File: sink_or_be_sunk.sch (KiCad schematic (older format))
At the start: 49 parts, among them J1 Battery_Conn, J10 SWD_Conn, J11 USB_B_Micro, J2 Display_Conn, J3 Keypad_Conn, J4 Mux_Conn, M1 Motor_DC, Q1 IRLML5203, Q2 MMBT5550L, Q3 MMBT5550L, SW4 Reset_SW, U1 ESP32-WROOM-32, U2 MCP608, U3 SN74HC151N, U6 LDL1117-SMD, U7 CY7C65213A-28PVXI, U8 MCP73831-2-OT

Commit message: cleaned up project
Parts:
- C1: renamed from C17; footprint Capacitor_SMD:C_0805_2012Metric_Pad1.15x1.40mm_HandSolder -> Capacitor_SMD:C_0805_2012Metric_Pad1.18x1.45mm_HandSolder
- C2: renamed from C18; footprint Capacitor_SMD:C_0805_2012Metric_Pad1.15x1.40mm_HandSolder -> Capacitor_SMD:C_0805_2012Metric_Pad1.18x1.45mm_HandSolder
- H1, H2, H3, H4: footprint MountingHole:MountingHole_6.4mm_M6 -> MountingHole:MountingHole_3.2mm_M3
- J6: renamed from J11; footprint digikey-footprints:USB_Micro_B_Female_Vert_1051330001 -> PCB_ESP32:USB_Micro_B_Female_Vert_1051330001
- R1, R2, R3: footprint Resistor_SMD:R_0805_2012Metric_Pad1.15x1.40mm_HandSolder -> Resistor_SMD:R_0805_2012Metric_Pad1.20x1.40mm_HandSolder
- R11: renamed from R22; footprint Resistor_SMD:R_0805_2012Metric_Pad1.15x1.40mm_HandSolder -> Resistor_SMD:R_0805_2012Metric_Pad1.20x1.40mm_HandSolder
- R7: renamed from R16; footprint Resistor_SMD:R_0805_2012Metric_Pad1.15x1.40mm_HandSolder -> Resistor_SMD:R_0805_2012Metric_Pad1.20x1.40mm_HandSolder
- R8: renamed from R17; footprint Resistor_SMD:R_0805_2012Metric_Pad1.15x1.40mm_HandSolder -> Resistor_SMD:R_0805_2012Metric_Pad1.20x1.40mm_HandSolder
- renumbered C22 to C10, C25 to C11, C23 to C3, C24 to C4, C19 to C5, C16 to C6, C1 to C7, C20 to C8, C21 to C9, D6 to D1, D1 to D2, D4 to D3, D5 to D4, J3 to J1, J4 to J2, J2 to J3, J10 to J4, J1 to J5, R19 to R10, R20 to R5, R21 to R6, R18 to R9, SW4 to SW1, U3 to U1, U6 to U2, U8 to U3, U2 to U4, U1 to U5, U7 to U6
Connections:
- net labels removed: VDD

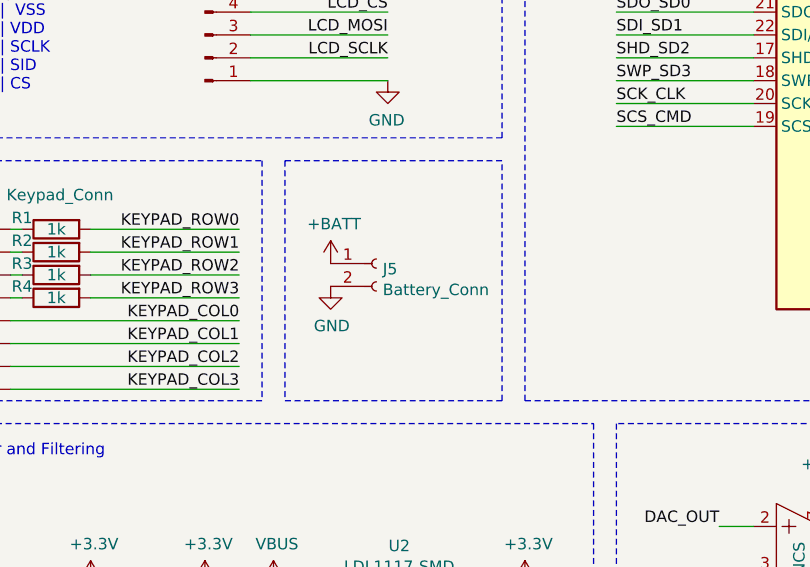
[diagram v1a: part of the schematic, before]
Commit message: added electrical isoltion switch
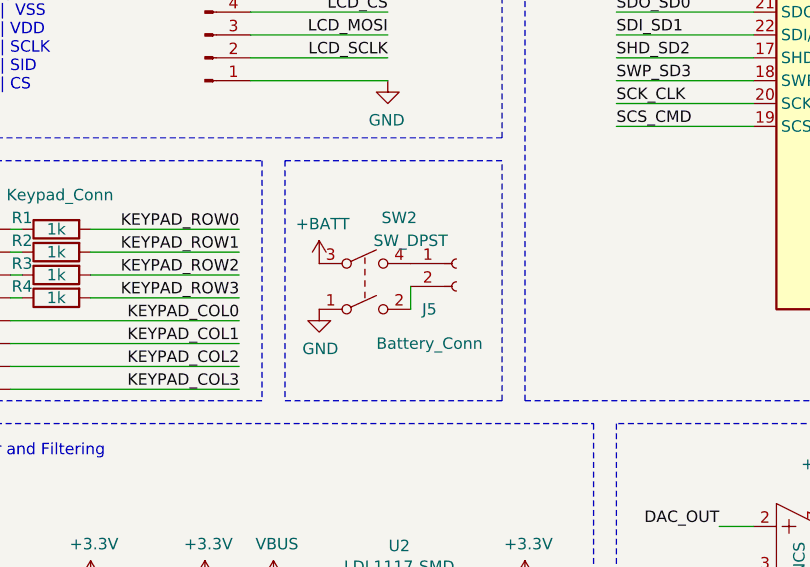
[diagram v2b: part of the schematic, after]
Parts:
- added SW2: SW_DPST, Connector_PinHeader_2.54mm:PinHeader_1x04_P2.54mm_Horizontal, symbol Switch:SW_DPST
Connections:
- wire segments 186 -> 187
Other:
- moved on the sheet: J5
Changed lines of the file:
@@
 L power:+BATT #PWR09
 U 1 1 622D2577
-P 2350 3350
-F 0 "#PWR09" H 2350 3200 50  0001 C CNN
-F 1 "+BATT" H 2365 3523 50  0000 C CNN
-F 2 "" H 2350 3350 50  0001 C CNN
-F 3 "" H 2350 3350 50  0001 C CNN
-	1    2350 3350
+P 2300 3350
+F 0 "#PWR09" H 2300 3200 50  0001 C CNN
+F 1 "+BATT" H 2315 3523 50  0000 C CNN
+F 2 "" H 2300 3350 50  0001 C CNN
+F 3 "" H 2300 3350 50  0001 C CNN
+	1    2300 3350
 	1    0    0    -1
 $EndComp
@@
 L power:GND #PWR010
 U 1 1 6239E5F9
-P 2350 3450
-F 0 "#PWR010" H 2350 3200 50  0001 C CNN
-F 1 "GND" H 2355 3277 50  0000 C CNN
-F 2 "" H 2350 3450 50  0001 C CNN
-F 3 "" H 2350 3450 50  0001 C CNN
-	1    2350 3450
+P 2300 3550
+F 0 "#PWR010" H 2300 3300 50  0001 C CNN
+F 1 "GND" H 2305 3377 50  0000 C CNN
+F 2 "" H 2300 3550 50  0001 C CNN
+F 3 "" H 2300 3550 50  0001 C CNN
+	1    2300 3550
 	1    0    0    -1
 $EndComp
@@
 L Connector:Conn_01x02_Female J5
 U 1 1 623CFEBF
-P 2550 3350
-F 0 "J5" H 2578 3326 50  0000 L CNN
-F 1 "Battery_Conn" H 2578 3235 50  0000 L CNN
-F 2 "Connector_JST:JST_PH_S2B-PH-K_1x02_P2.00mm_Horizontal" H 2550 3350 50  0001 C CNN
-F 3 "~" H 2550 3350 50  0001 C CNN
-	1    2550 3350
+P 2900 3350
+F 0 "J5" H 2750 3150 50  0000 L CNN
+F 1 "Battery_Conn" H 2550 3000 50  0000 L CNN
+F 2 "Connector_JST:JST_PH_S2B-PH-K_1x02_P2.00mm_Horizontal" H 2900 3350 50  0001 C CNN
+F 3 "~" H 2900 3350 50  0001 C CNN
+	1    2900 3350
 	1    0    0    -1
 $EndComp
@@
 	7400 5950 7650 5950
 $Comp
-L power:+3.3V #PWR?
+L power:+3.3V #PWR015
 U 1 1 61610F9E
 P 4500 4400
-F 0 "#PWR?" H 4500 4250 50  0001 C CNN
+F 0 "#PWR015" H 4500 4250 50  0001 C CNN
 F 1 "+3.3V" H 4515 4573 50  0000 C CNN
 F 2 "" H 4500 4400 50  0001 C CNN
@@
 	1    0    0    -1
 $EndComp
+$Comp
+L Switch:SW_DPST SW2
+U 1 1 615EE1A6
+P 2500 3450
+F 0 "SW2" H 2650 3750 50  0000 C CNN
+F 1 "SW_DPST" H 2700 3650 50  0000 C CNN
+F 2 "Connector_PinHeader_2.54mm:PinHeader_1x04_P2.54mm_Horizontal" H 2500 3450 50  0001 C CNN
+F 3 "~" H 2500 3450 50  0001 C CNN
+	1    2500 3450
+	1    0    0    -1
+$EndComp
+Wire Wire Line
+	2700 3450 2700 3550
 $EndSCHEMATC

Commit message: redo of layout and minor circuit updates
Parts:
- removed D2: D_Zener, Diode_SMD:D_0805_2012Metric_Pad1.15x1.40mm_HandSolder, symbol Device:D_Zener
- added C12: 10uF, Capacitor_THT:CP_Radial_D8.0mm_P3.50mm, symbol Device:C
- added D2: D, Diode_THT:D_DO-15_P10.16mm_Horizontal, symbol Device:D
- C7: footprint Capacitor_SMD:C_0805_2012Metric_Pad1.15x1.40mm_HandSolder -> Capacitor_THT:CP_Radial_D8.0mm_P3.50mm
- J4: value SWD_Conn -> JTAG_Conn; footprint Connector_PinHeader_2.54mm:PinHeader_1x06_P2.54mm_Vertical -> Connector_PinHeader_2.54mm:PinHeader_1x04_P2.54mm_Vertical; symbol Connector:Conn_01x06_Male -> Connector:Conn_01x04_Male
- U1: footprint PCB_ESP32:SN74HC151N-PDIP -> Package_DIP:DIP-16_W10.16mm
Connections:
- net labels added: MTCK, MTDI, MTDO, MTMS
- net labels removed: SCK_CLK, SCS_CMD, SDI_SD1, SDO_SD0, SHD_SD2, SWP_SD3
- wire segments 187 -> 182
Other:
- note removed: "Using 7/16” standoff \n(11.13mm tall, 6.35mm diam)"
- moved on the sheet: H1, H2, H3, H4
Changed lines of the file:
@@
-$EndComp
-$Comp
-L Device:D_Zener D?
-U 1 1 61603AE8
-P 7050 4100
-AR Path="/6154AAA6/61603AE8" Ref="D?"  Part="1"
-AR Path="/61603AE8" Ref="D2"  Part="1"
-F 0 "D2" V 7004 4179 50  0000 L CNN
-F 1 "D_Zener" V 7095 4179 50  0000 L CNN
-F 2 "Diode_SMD:D_0805_2012Metric_Pad1.15x1.40mm_HandSolder" H 7050 4100 50  0001 C CNN
-F 3 "~" H 7050 4100 50  0001 C CNN
-	1    7050 4100
-	0    1    1    0
 $EndComp
 $Comp
@@
 Wire Wire Line
 	5650 4900 5650 5050
-Wire Wire Line
-	5800 4750 6100 4750
 $Comp
 L Device:Speaker LS?
@@
 Text Label 3600 1050 0    50   ~ 0
 RESET
-Text Label 3600 2750 0    50   ~ 0
-SCS_CMD
-Text Label 3600 2650 0    50   ~ 0
-SCK_CLK
-Text Label 3600 2550 0    50   ~ 0
-SWP_SD3
-Text Label 3600 2450 0    50   ~ 0
-SHD_SD2
-Text Label 3600 2350 0    50   ~ 0
-SDI_SD1
-Text Label 3600 2250 0    50   ~ 0
-SDO_SD0
-Wire Wire Line
-	3600 2750 4200 2750
-Wire Wire Line
-	3600 2650 4200 2650
-Wire Wire Line
-	3600 2550 4200 2550
-Wire Wire Line
-	3600 2450 4200 2450
-Wire Wire Line
-	3600 2350 4200 2350
-Wire Wire Line
-	3600 2250 4200 2250
 Wire Wire Line
 	3600 1350 4200 1350
@@
 Wire Wire Line
 	5400 1250 6150 1250
-Text Label 6150 1650 2    50   ~ 0
+Text Label 3450 2350 0    50   ~ 0
 LED_OUT
 Wire Wire Line
-	5400 1650 6150 1650
+	4200 2350 3450 2350
 Text Label 6150 3150 2    50   ~ 0
 KEYPAD_COL3
@@
 Wire Wire Line
 	5400 2750 6150 2750
-Text Label 6150 1950 2    50   ~ 0
+Text Label 3450 2750 0    50   ~ 0
 LCD_CS
 Wire Wire Line
-	5400 1950 6150 1950
-Text Label 6150 1850 2    50   ~ 0
+	4200 2750 3450 2750
+Text Label 3450 2650 0    50   ~ 0
 LCD_SCLK
 Wire Wire Line
-	5400 1850 6150 1850
-Text Label 6150 1750 2    50   ~ 0
+	4200 2650 3450 2650
+Text Label 3450 2250 0    50   ~ 0
 LCD_MOSI
 Wire Wire Line
-	5400 1750 6150 1750
+	4200 2250 3450 2250
 Text Label 6150 2650 2    50   ~ 0
 MUX_ROW_SEL2
@@
 F 0 "C7" H 7765 6146 50  0000 L CNN
 F 1 "100uF" H 7765 6055 50  0000 L CNN
-F 2 "Capacitor_SMD:C_0805_2012Metric_Pad1.15x1.40mm_HandSolder" H 7688 5950 50  0001 C CNN
+F 2 "Capacitor_THT:CP_Radial_D8.0mm_P3.50mm" H 7688 5950 50  0001 C CNN
 F 3 "~" H 7650 6100 50  0001 C CNN
 	1    7650 6100
@@
 	7650 6250 7400 6250
 Connection ~ 7400 6250
-Text Label 2900 1400 2    50   ~ 0
-SCS_CMD
-Wire Wire Line
-	2900 1400 2300 1400
-Wire Wire Line
-	2900 900  2300 900
 Wire Wire Line
 	2900 1000 2300 1000
@@
 Wire Wire Line
 	2900 1300 2300 1300
-Text Label 2900 900  2    50   ~ 0
-SDO_SD0
 Text Label 2900 1000 2    50   ~ 0
-SDI_SD1
+MTDO
 Text Label 2900 1100 2    50   ~ 0
-SHD_SD2
+MTCK
 Text Label 2900 1200 2    50   ~ 0
-SWP_SD3
+MTDI
 Text Label 2900 1300 2    50   ~ 0
-SCK_CLK
-$Comp
-L Connector:Conn_01x06_Male J4
+MTMS
+$Comp
+L Connector:Conn_01x04_Male J4
 U 1 1 615AFA5D
 P 2100 1200
 F 0 "J4" H 2150 650 50  0000 R CNN
-F 1 "SWD_Conn" H 2300 750 50  0000 R CNN
-F 2 "Connector_PinHeader_2.54mm:PinHeader_1x06_P2.54mm_Vertical" H 2100 1200 50  0001 C CNN
+F 1 "JTAG_Conn" H 2300 750 50  0000 R CNN
+F 2 "Connector_PinHeader_2.54mm:PinHeader_1x04_P2.54mm_Vertical" H 2100 1200 50  0001 C CNN
 F 3 "~" H 2100 1200 50  0001 C CNN
 	1    2100 1200
@@
 F 0 "U1" H 2000 5885 50  0000 C CNN
 F 1 "SN74HC151N" H 2000 5976 50  0000 C CNN
-F 2 "PCB_ESP32:SN74HC151N-PDIP" H 2050 6450 50  0001 C CNN
+F 2 "Package_DIP:DIP-16_W10.16mm" H 2050 6450 50  0001 C CNN
 F 3 "" H 2050 6450 50  0001 C CNN
 	1    2000 6450
@@
 Wire Notes Line
 	6700 5650 3600 5650
-Text Notes 8400 5800 0    50   ~ 0
-Using 7/16” standoff \n(11.13mm tall, 6.35mm diam)
 $Comp
 L Mechanical:MountingHole H1
 U 1 1 6160EB38
-P 8500 6000
-F 0 "H1" H 8600 6046 50  0000 L CNN
-F 1 "MountingHole" H 8600 5955 50  0000 L CNN
-F 2 "MountingHole:MountingHole_3.2mm_M3" H 8500 6000 50  0001 C CNN
-F 3 "~" H 8500 6000 50  0001 C CNN
-	1    8500 6000
+P 8500 5900
+F 0 "H1" H 8600 5946 50  0000 L CNN
+F 1 "MountingHole" H 8600 5855 50  0000 L CNN
+F 2 "MountingHole:MountingHole_3.2mm_M3" H 8500 5900 50  0001 C CNN
+F 3 "~" H 8500 5900 50  0001 C CNN
+	1    8500 5900
 	1    0    0    -1
 $EndComp
@@
 L Mechanical:MountingHole H2
 U 1 1 615F8D16
-P 8500 6250
-F 0 "H2" H 8600 6296 50  0000 L CNN
-F 1 "MountingHole" H 8600 6205 50  0000 L CNN
-F 2 "MountingHole:MountingHole_3.2mm_M3" H 8500 6250 50  0001 C CNN
-F 3 "~" H 8500 6250 50  0001 C CNN
-	1    8500 6250
+P 8500 6150
+F 0 "H2" H 8600 6196 50  0000 L CNN
+F 1 "MountingHole" H 8600 6105 50  0000 L CNN
+F 2 "MountingHole:MountingHole_3.2mm_M3" H 8500 6150 50  0001 C CNN
+F 3 "~" H 8500 6150 50  0001 C CNN
+	1    8500 6150
 	1    0    0    -1
 $EndComp
@@
 L Mechanical:MountingHole H3
 U 1 1 615F8FBE
-P 9250 6000
-F 0 "H3" H 9350 6046 50  0000 L CNN
-F 1 "MountingHole" H 9350 5955 50  0000 L CNN
-F 2 "MountingHole:MountingHole_3.2mm_M3" H 9250 6000 50  0001 C CNN
-F 3 "~" H 9250 6000 50  0001 C CNN
-	1    9250 6000
+P 9250 5900
+F 0 "H3" H 9350 5946 50  0000 L CNN
+F 1 "MountingHole" H 9350 5855 50  0000 L CNN
+F 2 "MountingHole:MountingHole_3.2mm_M3" H 9250 5900 50  0001 C CNN
+F 3 "~" H 9250 5900 50  0001 C CNN
+	1    9250 5900
 	1    0    0    -1
 $EndComp
@@
 L Mechanical:MountingHole H4
 U 1 1 615F94F8
-P 9250 6250
-F 0 "H4" H 9350 6296 50  0000 L CNN
-F 1 "MountingHole" H 9350 6205 50  0000 L CNN
-F 2 "MountingHole:MountingHole_3.2mm_M3" H 9250 6250 50  0001 C CNN
-F 3 "~" H 9250 6250 50  0001 C CNN
-	1    9250 6250
+P 9250 6150
+F 0 "H4" H 9350 6196 50  0000 L CNN
+F 1 "MountingHole" H 9350 6105 50  0000 L CNN
+F 2 "MountingHole:MountingHole_3.2mm_M3" H 9250 6150 50  0001 C CNN
+F 3 "~" H 9250 6150 50  0001 C CNN
+	1    9250 6150
 	1    0    0    -1
 $EndComp
@@
 Wire Wire Line
 	2700 3450 2700 3550
+Wire Wire Line
+	6150 1650 5400 1650
+Text Label 6150 1650 2    50   ~ 0
+MTDI
+Wire Wire Line
+	6150 1750 5400 1750
+Text Label 6150 1750 2    50   ~ 0
+MTCK
+Wire Wire Line
+	6150 1850 5400 1850
+Text Label 6150 1850 2    50   ~ 0
+MTMS
+Wire Wire Line
+	6150 1950 5400 1950
+Text Label 6150 1950 2    50   ~ 0
+MTDO
+$Comp
+L Device:D D2
+U 1 1 616C0DF1
+P 7050 4100
+F 0 "D2" V 7004 4180 50  0000 L CNN
+F 1 "D" V 7095 4180 50  0000 L CNN
+F 2 "Diode_THT:D_DO-15_P10.16mm_Horizontal" H 7050 4100 50  0001 C CNN
+F 3 "https://www.diodes.com/assets/Datasheets/ds28002.pdf" H 7050 4100 50  0001 C CNN
+	1    7050 4100
+	0    1    1    0
+$EndComp
+$Comp
+L Device:C C12
+U 1 1 616DDA5F
+P 5950 4750
+F 0 "C12" V 5698 4750 50  0000 C CNN
+F 1 "10uF" V 5789 4750 50  0000 C CNN
+F 2 "Capacitor_THT:CP_Radial_D8.0mm_P3.50mm" H 5988 4600 50  0001 C CNN
+F 3 "~" H 5950 4750 50  0001 C CNN
+	1    5950 4750
+	0    1    1    0
+$EndComp
 $EndSCHEMATC

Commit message: 10/7 organizing ratsnest more
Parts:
- removed D3, D4: LED, LED_THT:LED_D3.0mm, symbol Device:LED
- removed R10, R9: 1k, Resistor_SMD:R_0805_2012Metric_Pad1.15x1.40mm_HandSolder, symbol Device:R
- added D5: D, Diode_THT:D_DO-15_P10.16mm_Horizontal, symbol Device:D
- added J7: JTAG_Conn, Connector_PinHeader_2.54mm:PinHeader_1x02_P2.54mm_Vertical, symbol Connector:Conn_01x02_Male
- added Q4: Q_PMOS_DGS, Package_TO_SOT_THT:TO-220-3_Vertical, symbol Device:Q_PMOS_DGS
- added R12: 100k, Resistor_SMD:R_0805_2012Metric_Pad1.15x1.40mm_HandSolder, symbol Device:R
- added TP1, TP2: TestPoint, TestPoint:TestPoint_Pad_2.0x2.0mm, symbol Connector:TestPoint
- J3: footprint Connector_PinHeader_2.54mm:PinHeader_1x05_P2.54mm_Horizontal -> Connector_PinHeader_2.54mm:PinHeader_1x05_P2.54mm_Vertical
- LS1, SW1: footprint Connector_PinHeader_2.54mm:PinHeader_1x02_P2.54mm_Horizontal -> Connector_PinHeader_2.54mm:PinHeader_1x02_P2.54mm_Vertical
- Q1: footprint Package_TO_SOT_SMD:SOT-23 -> Package_TO_SOT_THT:TO-220-3_Vertical
- Q2, Q3: value MMBT5550L -> 2N3704; footprint Package_TO_SOT_SMD:SOT-23 -> Package_TO_SOT_THT:TO-92; symbol Transistor_BJT:MMBT5550L -> Device:Q_NPN_ECB
- RV1: footprint Connector_PinHeader_2.54mm:PinHeader_1x03_P2.54mm_Horizontal -> Connector_PinHeader_2.54mm:PinHeader_1x03_P2.54mm_Vertical
- SW2: footprint Connector_PinHeader_2.54mm:PinHeader_1x04_P2.54mm_Horizontal -> Connector_PinHeader_2.54mm:PinHeader_1x04_P2.54mm_Vertical
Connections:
- net +BATT: now also Q4.1 (D)
- net BOAT_INPUT: now also U5.27 (IO16); no longer U5.6 (IO34)
- net DTR: now also Q2.1 (E); no longer Q2.2 (E)
- net GND: now also R12.2
- net GPIO0: now also Q2.2 (C); no longer Q2.3 (C)
- net KEYPAD_COL0: now also J1.1 (Pin_1), U5.24 (IO2); no longer J1.5 (Pin_5), U5.11 (IO26)
- net KEYPAD_COL1: now also J1.2 (Pin_2), U5.22 (SDI/SD1); no longer J1.6 (Pin_6), U5.12 (IO27)
- net KEYPAD_COL2: now also J1.3 (Pin_3), U5.18 (SWP/SD3); no longer J1.7 (Pin_7), U5.8 (IO32)
- net KEYPAD_COL3: now also J1.4 (Pin_4), U5.17 (SHD/SD2); no longer J1.8 (Pin_8), U5.9 (IO33)
- net KEYPAD_ROW0: now also U5.12 (IO27); no longer U5.27 (IO16)
- net KEYPAD_ROW1: now also U5.11 (IO26); no longer U5.28 (IO17)
- net KEYPAD_ROW2: now also U5.9 (IO33); no longer U5.30 (IO18)
- net KEYPAD_ROW3: now also U5.8 (IO32); no longer U5.31 (IO19)
- net LCD_MOSI: now also J3.2 (Pin_2); no longer J3.3 (Pin_3)
- net LCD_SCLK: now also J3.3 (Pin_3); no longer J3.2 (Pin_2)
- net LED_OUT: now also U5.37 (IO23); no longer U5.22 (SDI/SD1)
- net MOTOR: now also U5.26 (IO4); no longer U5.7 (IO35)
- net MUX_COL_SEL0: now also U5.30 (IO18); no longer U5.24 (IO2)
- net MUX_COL_SEL1: now also U5.29 (IO5); no longer U5.26 (IO4)
- net MUX_COL_SEL2: now also U5.28 (IO17); no longer U5.29 (IO5)
- net MUX_ROW0: now also J2.4 (Pin_4); no longer J2.1 (Pin_1)
- net MUX_ROW1: now also J2.3 (Pin_3); no longer J2.2 (Pin_2)
- net MUX_ROW2: now also J2.2 (Pin_2); no longer J2.3 (Pin_3)
- net MUX_ROW3: now also J2.1 (Pin_1); no longer J2.4 (Pin_4)
- net MUX_ROW_SEL0: now also U5.31 (IO19); no longer U5.33 (IO21)
- net MUX_ROW_SEL1: now also U5.33 (IO21); no longer U5.36 (IO22)
- net MUX_ROW_SEL2: now also U5.36 (IO22); no longer U5.37 (IO23)
- net RESET: now also Q3.2 (C); no longer Q3.3 (C)
- net RTS: now also Q3.1 (E); no longer Q3.2 (E)
- net RXLED: now also TP1.1
- net TXLED: now also TP2.1
- net VBUS: now also D5.2 (A), Q4.2 (G), R12.1; no longer U2.3 (VIN)
- net VCCD4: now reaches C5.1, U6.17 (VCCD)
- net at R1.1: now also J1.5 (Pin_5); no longer J1.1 (Pin_1)
- net at R2.1: now also J1.6 (Pin_6); no longer J1.2 (Pin_2)
- net at R3.1: now also J1.7 (Pin_7); no longer J1.3 (Pin_3)
- net at R4.1: now also J1.8 (Pin_8); no longer J1.4 (Pin_4)
- net at SW2.2: now also J5.1 (Pin_1); no longer J5.2 (Pin_2)
- net at SW2.4: now also J5.2 (Pin_2); no longer J5.1 (Pin_1)
- net at R7.1: now also Q2.3 (B); no longer Q2.1 (B)
- net at R8.1: now also Q3.3 (B); no longer Q3.1 (B)
- new net: D5.1 (K), Q4.3 (S), U2.3 (VIN)
- new net DBG1: J7.1 (Pin_1), U5.6 (IO34)
- new net DBG2: J7.2 (Pin_2), U5.7 (IO35)
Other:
- moved on the sheet: C1, C2, J1, R1, R2, R3, R4, U2, U5

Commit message: updated with todos from talk with prof
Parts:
- added D?: LED, LED_THT:LED_D3.0mm, symbol Device:LED
- added R?: 470, Resistor_SMD:R_0805_2012Metric_Pad1.15x1.40mm_HandSolder, symbol Device:R
- added R? (x2): 20, symbol Device:R
- J7: value JTAG_Conn -> Debug_Conn
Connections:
- net +3V3: now also D?.2 (A)
- net GND: now also R?.2
- net MTDO: now also R?.1; no longer J4.4 (Pin_4)
- net MUX_ROW3: now also R?.2
- new net: J4.4 (Pin_4), R?.2
- new net: D?.1 (K), R?.1
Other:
- note added: "Big Via for pad 39 GND on Esp module for soldering"
- note added: "Mounting Holes"
- note added: "R for\nESD Protection\n"
- note added: "TODO: \n- 20 ohm for JTAG, MUX\n- connectors for all 16 grid boards\n- big via for gnd pad on esp\n- heat calcs for LDO, MOSFET in Power and filtering section, speaker\n- test speaker circuit for sound volume"
- note added: "need headers to Grid PCB"
- note removed: "TODO: \n\n- Connect the sheets \n(mitch, you might have to help me with this)\n\n- maybe add an external ocillator spot like they suggested?\n\n- Add a voltage src (probably a boost converter) for the 5V motor"
- moved on the sheet: C1, C2, D1, D5, J1, J3, J5, J7, Q4, R1, R12, R2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
